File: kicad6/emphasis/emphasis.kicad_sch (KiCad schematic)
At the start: 24 parts, among them J1 EMPH_IN, J10 Conn_01x03_Female, J11 Conn_01x03_Male, J12 Conn_01x03_Male, J13 Conn_01x20_Male, J14 Conn_02x05, J2 DIST_IN, J3 DE_EMPH_IN, J4 EMPH_OUT, J5 DIST_OUT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

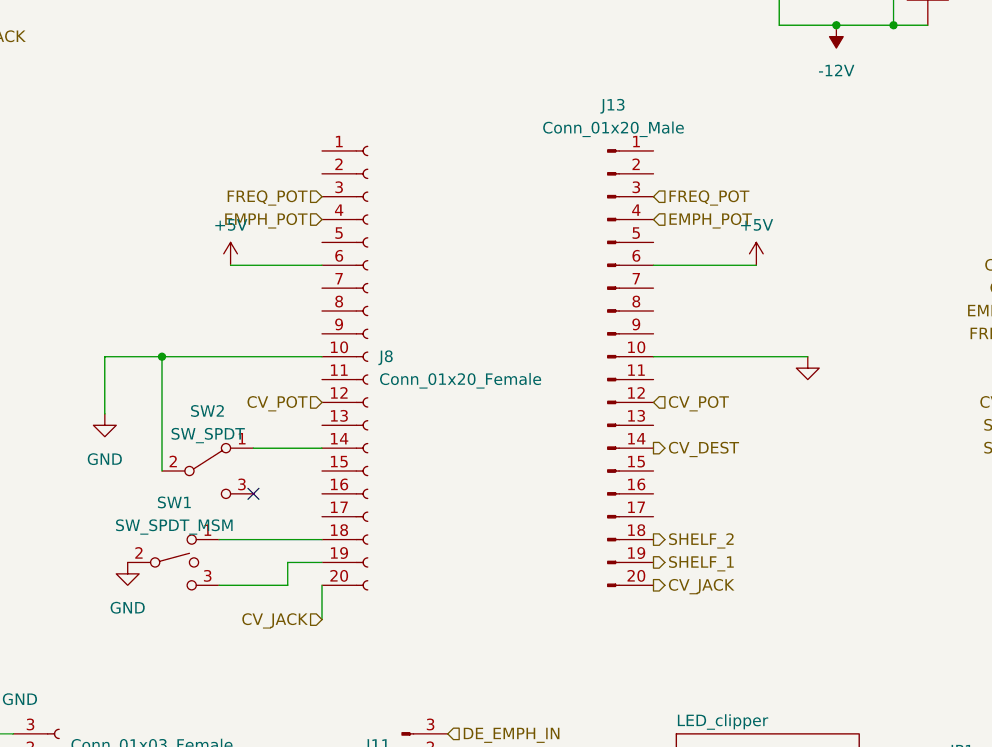
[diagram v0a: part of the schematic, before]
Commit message: emphasis pin shuffling
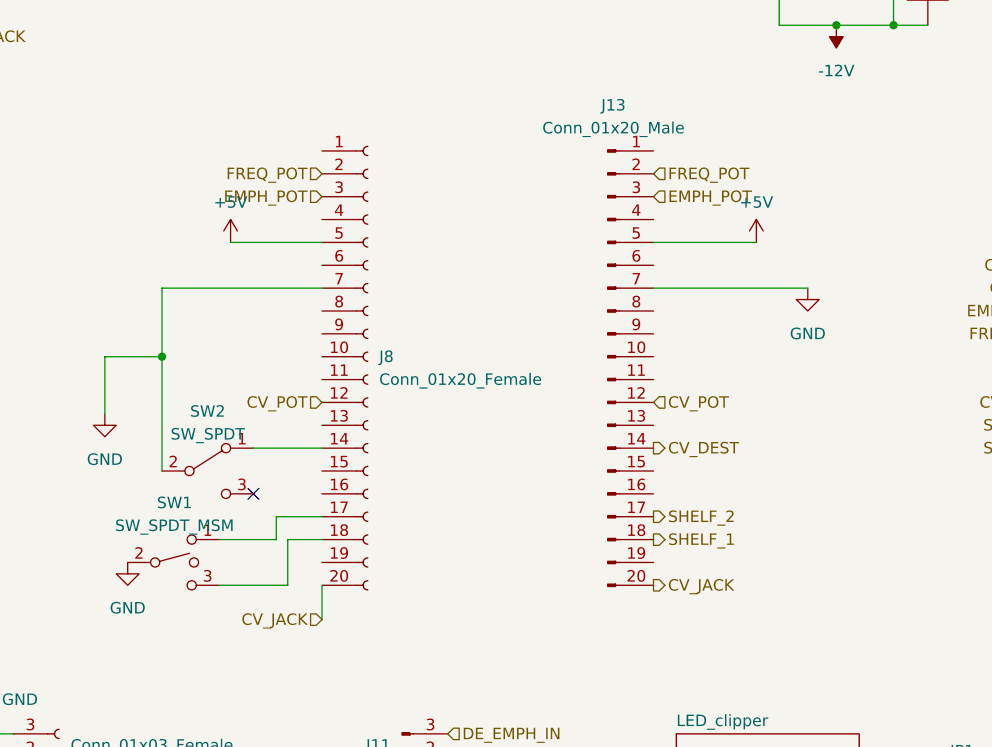
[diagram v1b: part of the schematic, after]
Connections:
- net +5V: now also J13.5 (Pin_5), J8.5 (Pin_5); no longer J13.6 (Pin_6), J8.6 (Pin_6)
- net EMPH_POT: now also J13.3 (Pin_3), J8.3 (Pin_3); no longer J13.4 (Pin_4), J8.4 (Pin_4)
- net FREQ_POT: now also J13.2 (Pin_2), J8.2 (Pin_2); no longer J13.3 (Pin_3), J8.3 (Pin_3)
- net GND: now also J13.7 (Pin_7), J8.7 (Pin_7); no longer J13.10 (Pin_10), J8.10 (Pin_10)
- net SHELF_1: now also J13.18 (Pin_18); no longer J13.19 (Pin_19)
- net SHELF_2: now also J13.17 (Pin_17); no longer J13.18 (Pin_18)
- net at J8.17 (Pin_17): now also SW1.1
- net at J8.18 (Pin_18): now also SW1.3; no longer SW1.1
- net at J8.19 (Pin_19): no longer SW1.3

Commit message: Emphasis: flipped board, take 1
Not entirely happy with the way this is going, might start again.

Basically I messed up the orientation of the main board relative to
the control board: to avoid having the patch_sm stick out the side,
parts need to be mounted on the "back" of main board. But this flips
the orientation of patch_sm and ICs, so everything needs to be
re-routed.
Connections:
- net CV_DEST: now also U1.D3 (SDMMC_D2); no longer U1.D7 (SDMMC_CMD)
- net CV_JACK: now also U1.C9 (CV8); no longer U1.C6 (CV5)
- net CV_POT: now also U1.C8 (CV7); no longer U1.C7 (CV6)
- net EMPH_POT: now also U1.C7 (CV6); no longer U1.C8 (CV7)
- net FREQ_POT: now also U1.C6 (CV5); no longer U1.C9 (CV8)
- net SHELF_1: now also U1.D5 (SDMMC_D0); no longer U1.D4 (SDMMC_D1)
- net SHELF_2: now also U1.D4 (SDMMC_D1); no longer U1.D5 (SDMMC_D0)
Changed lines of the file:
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@@
     (effects (font (size 1.27 1.27)) (justify left))
   )
-  (hierarchical_label "CV_POT" (shape input) (at 218.44 78.74 180)
+  (hierarchical_label "CV_POT" (shape input) (at 218.44 81.28 180)
     (effects (font (size 1.27 1.27)) (justify right))
   )
@@
     (effects (font (size 1.27 1.27)) (justify left))
   )
-  (hierarchical_label "SHELF_2" (shape input) (at 218.44 93.98 180)
+  (hierarchical_label "SHELF_2" (shape input) (at 218.44 96.52 180)
     (effects (font (size 1.27 1.27)) (justify right))
   )
@@
     (effects (font (size 1.27 1.27)) (justify right))
   )
-  (hierarchical_label "FREQ_POT" (shape input) (at 218.44 83.82 180)
+  (hierarchical_label "FREQ_POT" (shape input) (at 218.44 76.2 180)
     (effects (font (size 1.27 1.27)) (justify right))
   )
@@
     (effects (font (size 1.27 1.27)) (justify left))
   )
-  (hierarchical_label "SHELF_1" (shape input) (at 218.44 96.52 180)
+  (hierarchical_label "SHELF_1" (shape input) (at 218.44 93.98 180)
     (effects (font (size 1.27 1.27)) (justify right))
   )
@@
     (effects (font (size 1.27 1.27)) (justify left))
   )
-  (hierarchical_label "CV_JACK" (shape input) (at 218.44 76.2 180)
+  (hierarchical_label "CV_JACK" (shape input) (at 218.44 83.82 180)
     (effects (font (size 1.27 1.27)) (justify right))
   )
-  (hierarchical_label "CV_DEST" (shape input) (at 218.44 91.44 180)
+  (hierarchical_label "CV_DEST" (shape input) (at 218.44 99.06 180)
     (effects (font (size 1.27 1.27)) (justify right))
   )
@@
     (effects (font (size 1.27 1.27)) (justify right))
   )
-  (hierarchical_label "EMPH_POT" (shape input) (at 218.44 81.28 180)
+  (hierarchical_label "EMPH_POT" (shape input) (at 218.44 78.74 180)
     (effects (font (size 1.27 1.27)) (justify right))
   )

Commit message: Emphasis take 3: flipped components, cleaner layout
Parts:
- added JP3, JP4: Jumper_2_Bridged, Connector_PinHeader_2.54mm:PinHeader_1x02_P2.54mm_Vertical, symbol Jumper:Jumper_2_Bridged
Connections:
- net CV_DEST: now also U1.D5 (SDMMC_D0); no longer U1.D3 (SDMMC_D2)
- net DE_EMPH_OUT: now also J12.1 (Pin_1); no longer J12.3 (Pin_3)
- net EMPH_OUT: now also J12.3 (Pin_3); no longer J12.1 (Pin_1)
- net GND: now also JP3.2 (B), JP4.2 (B)
- net SHELF_1: now also U1.D7 (SDMMC_CMD); no longer U1.D5 (SDMMC_D0)
- net SHELF_2: now also U1.D6 (SDMMC_CK); no longer U1.D4 (SDMMC_D1)
- net at U1.D1 (SPI_NSS): now also JP3.1 (A)
- net at U1.D10 (SPI_SCK): now also JP4.1 (A)
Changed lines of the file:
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@@
   (junction (at 199.39 39.37) (diameter 0) (color 0 0 0 0)
+  )
+  (junction (at 274.32 119.38) (diameter 0) (color 0 0 0 0)
   )
   (no_connect (at 95.25 152.4))
@@
     (stroke (width 0) (type default) (color 0 0 0 0))
   )
+  (wire (pts (xy 274.32 111.76) (xy 274.32 119.38))
+    (stroke (width 0) (type default) (color 0 0 0 0))
+  )
   (wire (pts (xy 199.39 39.37) (xy 203.2 39.37))
     (stroke (width 0) (type default) (color 0 0 0 0))
   )
+  (wire (pts (xy 259.08 119.38) (xy 264.16 119.38))
+    (stroke (width 0) (type default) (color 0 0 0 0))
+  )
   (wire (pts (xy 55.88 118.11) (xy 64.77 118.11))
     (stroke (width 0) (type default) (color 0 0 0 0))
@@
   )
   (wire (pts (xy 186.69 44.45) (xy 186.69 49.53))
+    (stroke (width 0) (type default) (color 0 0 0 0))
+  )
+  (wire (pts (xy 259.08 111.76) (xy 264.16 111.76))
     (stroke (width 0) (type default) (color 0 0 0 0))
   )
@@
     (effects (font (size 1.27 1.27)) (justify left))
   )
-  (hierarchical_label "SHELF_2" (shape input) (at 218.44 96.52 180)
+  (hierarchical_label "SHELF_2" (shape input) (at 218.44 88.9 180)
     (effects (font (size 1.27 1.27)) (justify right))
   )
@@
     (effects (font (size 1.27 1.27)) (justify left))
   )
-  (hierarchical_label "SHELF_1" (shape input) (at 218.44 93.98 180)
+  (hierarchical_label "SHELF_1" (shape input) (at 218.44 91.44 180)
     (effects (font (size 1.27 1.27)) (justify right))
   )
@@
     (effects (font (size 1.27 1.27)) (justify right))
   )
-  (hierarchical_label "CV_DEST" (shape input) (at 218.44 99.06 180)
+  (hierarchical_label "CV_DEST" (shape input) (at 218.44 93.98 180)
     (effects (font (size 1.27 1.27)) (justify right))
   )
@@
     (pin "9")
   )
+  (symbol (lib_id "Jumper:Jumper_2_Bridged") (at 269.24 119.38 0) (unit 1)
+    (in_bom yes) (on_board yes) (fields_autoplaced)
+    (property "Reference" "JP4" (id 0) (at 269.24 113.665 0))
+    (property "Value" "Jumper_2_Bridged" (id 1) (at 269.24 116.205 0))
+    (property "Footprint" "Connector_PinHeader_2.54mm:PinHeader_1x02_P2.54mm_Vertical" (id 2) (at 269.24 119.38 0)
+      (effects (font (size 1.27 1.27)) hide)
+    )
+    (property "Datasheet" "~" (id 3) (at 269.24 119.38 0)
+      (effects (font (size 1.27 1.27)) hide)
+    )
+    (pin "1")
+    (pin "2")
+  )
   (symbol (lib_id "power:GND") (at 111.76 92.71 0) (unit 1)
     (in_bom yes) (on_board yes) (fields_autoplaced)
@@
     (pin "1")
   )
-  (symbol (lib_id "Connector:Conn_01x03_Male") (at 144.78 152.4 0) (mirror x) (unit 1)
-    (in_bom yes) (on_board yes) (fields_autoplaced)
-    (property "Reference" "J12" (id 0) (at 143.51 151.1299 0)
-      (effects (font (size 1.27 1.27)) (justify right))
-    )
-    (property "Value" "Conn_01x03_Male" (id 1) (at 143.51 153.6699 0)
-      (effects (font (size 1.27 1.27)) (justify right))
-    )
+  (symbol (lib_id "Jumper:Jumper_2_Bridged") (at 269.24 111.76 0) (unit 1)
+    (in_bom yes) (on_board yes) (fields_autoplaced)
+    (property "Reference" "JP3" (id 0) (at 269.24 106.045 0))
+    (property "Value" "Jumper_2_Bridged" (id 1) (at 269.24 108.585 0))
+    (property "Footprint" "Connector_PinHeader_2.54mm:PinHeader_1x02_P2.54mm_Vertical" (id 2) (at 269.24 111.76 0)
+      (effects (font (size 1.27 1.27)) hide)
+    )
+    (property "Datasheet" "~" (id 3) (at 269.24 111.76 0)
+      (effects (font (size 1.27 1.27)) hide)
+    )
+    (pin "1")
+    (pin "2")
+  )
+  (symbol (lib_id "Connector:Conn_01x03_Male") (at 144.78 152.4 0) (unit 1)
+    (in_bom yes) (on_board yes) (fields_autoplaced)
+    (property "Reference" "J12" (id 0) (at 145.415 146.084 0))
+    (property "Value" "Conn_01x03_Male" (id 1) (at 145.415 148.6209 0))
     (property "Footprint" "Connector_Molex:Molex_KK-254_AE-6410-03A_1x03_P2.54mm_Vertical" (id 2) (at 144.78 152.4 0)
       (effects (font (size 1.27 1.27)) hide)
@@
     (pin "2")
     (pin "3")
+  )
+  (symbol (lib_id "power:GND") (at 274.32 119.38 0) (unit 1)
+    (in_bom yes) (on_board yes) (fields_autoplaced)
+    (property "Reference" "#PWR08" (id 0) (at 274.32 125.73 0)
+      (effects (font (size 1.27 1.27)) hide)
+    )
+    (property "Value" "GND" (id 1) (at 274.32 124.46 0))
+    (property "Footprint" "" (id 2) (at 274.32 119.38 0)
+      (effects (font (size 1.27 1.27)) hide)
+    )
+    (property "Datasheet" "" (id 3) (at 274.32 119.38 0)
+      (effects (font (size 1.27 1.27)) hide)
+    )
+    (pin "1")
   )
   (sheet (at 175.26 128.27) (size 20.32 29.21) (fields_autoplaced)
@@
       (reference "#PWR07") (unit 1) (value "GND") (footprint "")
     )
+    (path "/ffe97c1a-26ee-44fc-87a5-4ced6301528b"
+      (reference "#PWR08") (unit 1) (value "GND") (footprint "")
+    )
     (path "/7c5f35ec-8b03-442d-bd51-c64fed8b2c39"
       (reference "#PWR0101") (unit 1) (value "GND") (footprint "")
@@
       (reference "JP2") (unit 1) (value "Jumper_2_Bridged") (footprint "Connector_PinHeader_2.54mm:PinHeader_1x02_P2.54mm_Vertical")
     )
+    (path "/ce852650-8e48-4e56-a4aa-ffd7ce34212b"
+      (reference "JP3") (unit 1) (value "Jumper_2_Bridged") (footprint "Connector_PinHeader_2.54mm:PinHeader_1x02_P2.54mm_Vertical")
+    )
+    (path "/a28a9088-e63c-4b09-ba04-3ade5cb32856"
+      (reference "JP4") (unit 1) (value "Jumper_2_Bridged") (footprint "Connector_PinHeader_2.54mm:PinHeader_1x02_P2.54mm_Vertical")
+    )
     (path "/76d7d707-d099-4c2f-b0f4-f35fc503e70f/63bfdbbf-202c-4761-bbe1-b3126ec382e0"
